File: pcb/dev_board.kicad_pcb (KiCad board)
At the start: 6 copper layers, 45.7 x 50 mm, 42 parts, among them J1 Conn_02x13_Odd_Even, J2 Conn_02x13_Odd_Even, J4 Conn_01x05, J5 Screw_Terminal_01x03, Q1 Si2356DS, Q2 Si2356DS, Q5 2N3906, Q6 MMBT3904, Q7 MMBT3906, SW1 SW_DIP_x04, U1 XS-LDT-01, U2 MAX5026, U3 KXTJ3-1057, U4 MCP1640BCH, U6 TLV74311

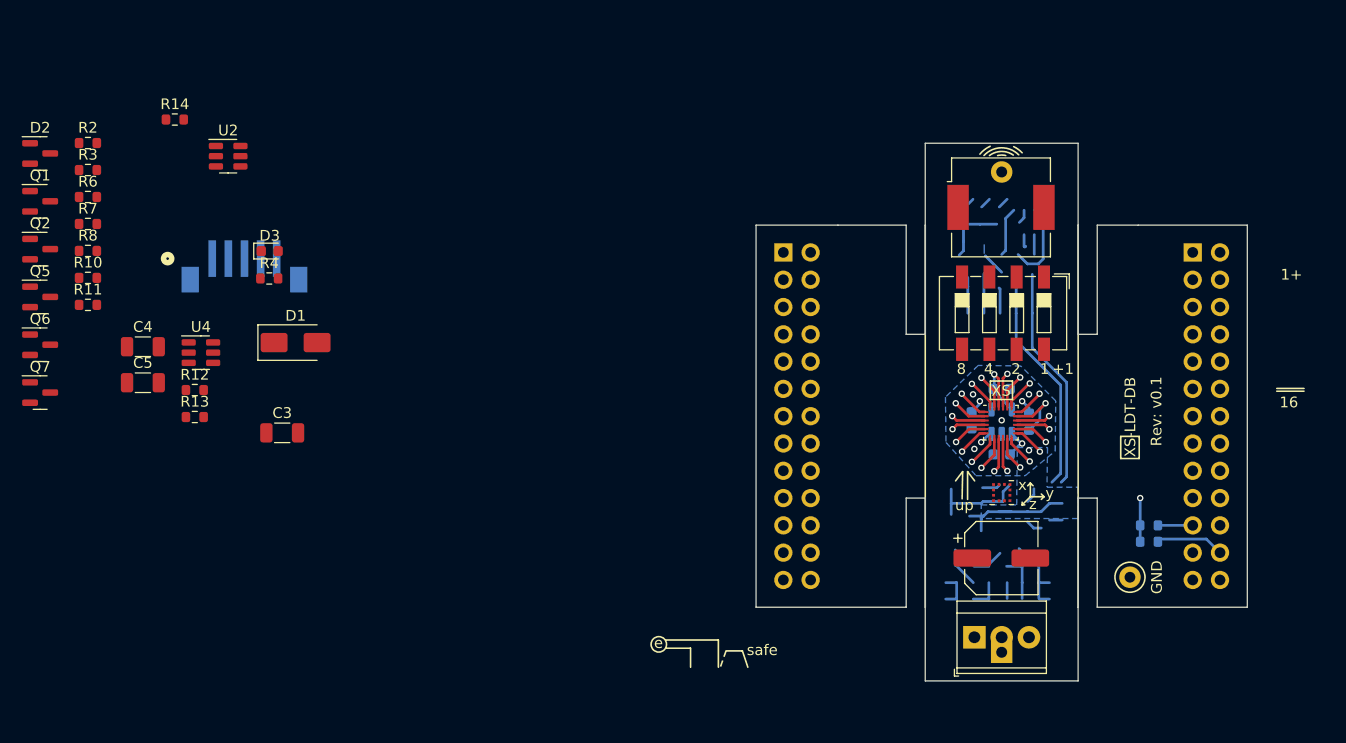
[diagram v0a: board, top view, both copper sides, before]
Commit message: V0.2 pcb placement, good enough to proceed/.
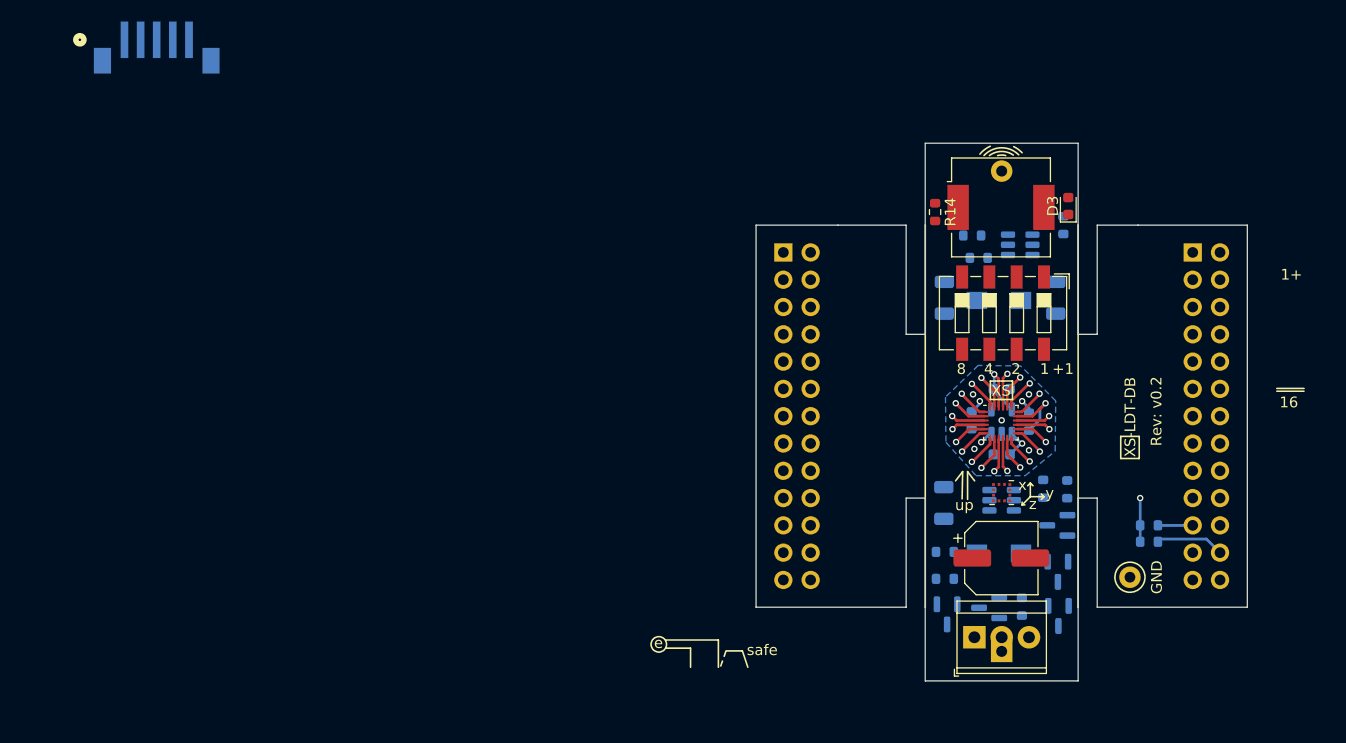
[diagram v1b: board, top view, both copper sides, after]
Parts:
- removed D1: ES1J, Diode_SMD:D_SMA
- removed Q5: 2N3906, Package_TO_SOT_SMD:SOT-23
- removed R2: 10K, Resistor_SMD:R_0603_1608Metric
- removed R6: 100K, Resistor_SMD:R_0603_1608Metric
- added L1: 47uH, Inductor_SMD:L_Wuerth_HCI-5040, B.Cu at (169.9, 116.9)
- added L2: 4.7uH, Inductor_SMD:L_Wuerth_HCI-5040, B.Cu at (169.9, 93.4)
- C3, C4, C5, D2, Q1, Q2, Q6, Q7, R10, R11, R12, R13, R3, R4, R7, R8, U2, U4: moved to B.Cu
- moved D2 100.8 mm to (175.4, 114.3), turned to 180 degrees
- moved Q2 100.7 mm to (175.5, 122.7), turned to -90 degrees
- moved Q7 96.2 mm to (175.4, 118.6), turned to -90 degrees
- moved R3 95.9 mm to (172.1, 121.9), turned to -90 degrees
- moved R10 93.2 mm to (176.3, 110.9), turned to -90 degrees
- moved Q1 92.7 mm to (165.1, 122.6), turned to -90 degrees
- moved Q6 91.6 mm to (169.0, 122.0), turned to 180 degrees
- moved R11 90.5 mm to (174.0, 110.9), turned to -90 degrees
- moved R7 85.4 mm to (164.9, 116.8), turned to 180 degrees
- moved R8 85.4 mm to (164.9, 119.3), turned to 180 degrees
- moved C5 85.3 mm to (175.2, 93.1), turned to -90 degrees
- moved U2 78.8 mm to (170.2, 112.0), turned to 180 degrees
- moved U4 76.9 mm to (171.9, 88.2), turned to 180 degrees
- moved C4 74.7 mm to (164.8, 93.1), turned to -90 degrees
- moved D3 74.4 mm to (176.4, 84.6), turned to 90 degrees
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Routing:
- net (no net): track 72.6 -> 16.4 mm
- net GND: track 31.9 -> 6.08 mm
- net unconnected-(J5-Pin_3-Pad3): track 18.5 -> 0.00 mm
- net unconnected-(J5-Pin_1-Pad1): track 15.3 -> 0.00 mm
- net +3.3V: track 21.0 -> 9.98 mm
- net /out: track 3.69 -> 0.00 mm
- net /pump: track 26.3 -> 23.3 mm
- net Net-(D3-K): track 1.02 -> 0.00 mm

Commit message: V0.3 schematic complete, footprints, 3d mods, prelim plancement. Ready for review then routing.
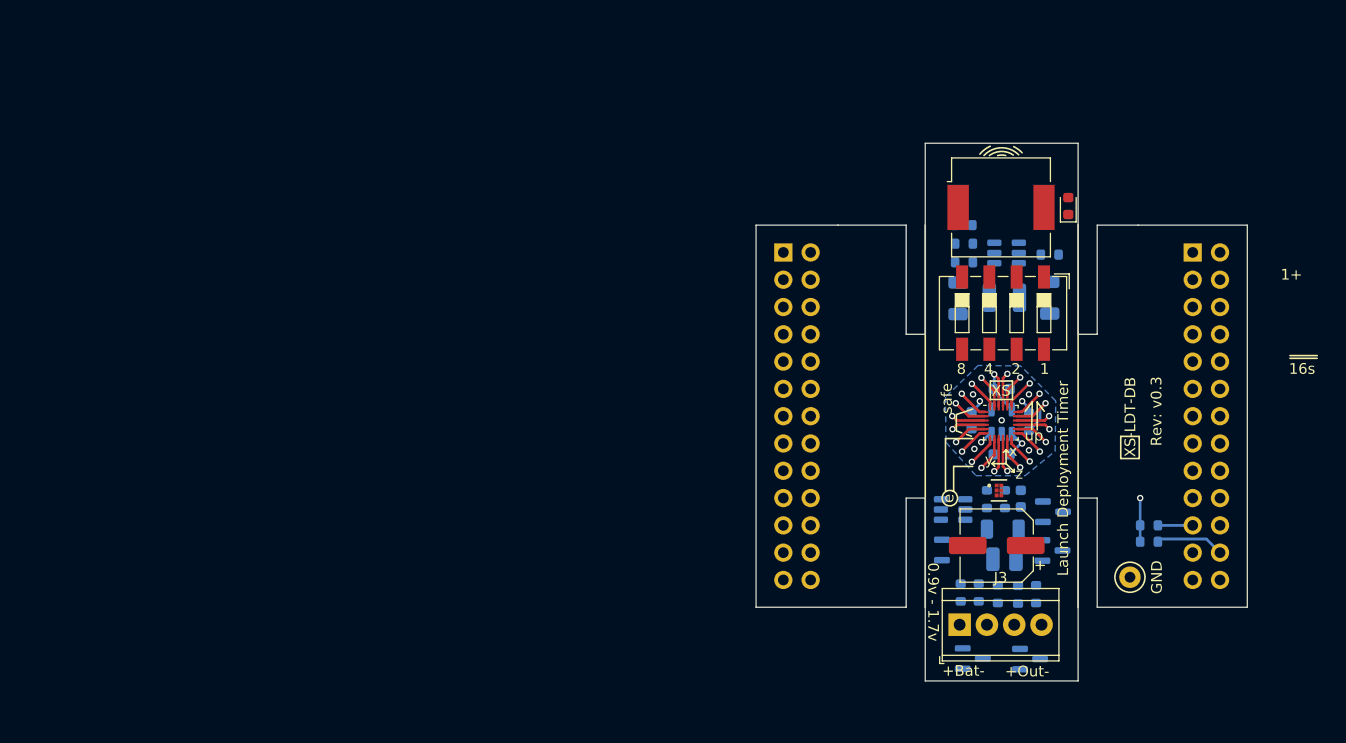
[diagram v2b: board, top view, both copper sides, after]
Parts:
- removed BT1: AAA Battery, Battery:BatteryHolder_Keystone_2466_1xAAA
- removed J4: Conn_01x05, Connector_JST:CONN_B5B-ZR-SM4-TF_JST
- removed J5: Screw_Terminal_01x03, TerminalBlock_TE-Connectivity:TerminalBlock_TE_282834-3_1x03_P2.54mm_Horizontal
- added C6: 1u, Capacitor_SMD:C_0603_1608Metric, B.Cu at (172.0, 111.8)
- added J3: Screw_Terminal_01x04, TerminalBlock_TE-Connectivity:TerminalBlock_TE_282834-4_1x04_P2.54mm_Horizontal, F.Cu at (166.3, 123.5)
- added R2: 3K3, Resistor_SMD:R_0603_1608Metric, B.Cu at (170.5, 111.9)
- added R6: 3K3, Resistor_SMD:R_0603_1608Metric, B.Cu at (168.8, 111.9)
- D2: value BAV99 -> CD0603-B0340R
- L1: footprint Inductor_SMD:L_Wuerth_HCI-5040 -> Inductor_SMD:L_1008_2520Metric
- L2: footprint Inductor_SMD:L_Wuerth_HCI-5040 -> Inductor_SMD:L_1210_3225Metric
- LS1: value Speaker -> Piezo
- R10: value 100K -> 147K
- R11: value 10K -> 6K34
- R12: value 100K -> 976K
- R13: value 10K -> 562K
- R14: moved to B.Cu
- U3: value KXTJ3-1057 -> MXC4005XC; footprint Package_LGA:Kionix_LGA-12_2x2mm_P0.5mm_LayoutBorder2x4y -> Sensor:MXC4005XC_MEM-M
- moved R11 12.3 mm to (166.4, 120.5), turned to 90 degrees
- moved R10 10.2 mm to (173.4, 120.7), turned to 90 degrees
- moved Q6 6.40 mm to (165.6, 116.6), turned to 0 degrees
- moved C3 6.00 mm to (170.3, 114.7), turned to 0 degrees
- moved R8 5.13 mm to (169.8, 120.7), turned to -90 degrees
- moved R7 4.92 mm to (168.0, 120.5), turned to -90 degrees
- moved Q2 4.80 mm to (172.8, 126.7), turned to 0 degrees
- moved Q1 4.76 mm to (167.5, 126.7), turned to 0 degrees
- moved U2 4.60 mm to (165.7, 112.8)
- moved R4 3.02 mm to (174.7, 89.1), turned to 0 degrees
- moved R14 2.91 mm to (166.6, 86.4), turned to 0 degrees
- moved Q7 2.05 mm to (174.9, 116.6), turned to 0 degrees
- moved U4 1.48 mm to (170.6, 89.0)
- moved R12 1.43 mm to (166.7, 89.8)
- moved D2 1.33 mm to (175.0, 113.0), turned to 0 degrees
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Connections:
- C1 pad 1: unconnected-(C1-Pad1) -> /cap_30v
- C1 pad 2: unconnected-(C1-Pad2) -> GND
- C3 pad 1: unconnected-(C3-Pad1) -> +3.3V
- C3 pad 2: unconnected-(C3-Pad2) -> GND
- C4 pad 1: unconnected-(C4-Pad1) -> +BATT
- C4 pad 2: unconnected-(C4-Pad2) -> GND
- C5 pad 1: unconnected-(C5-Pad1) -> +3.3V
- C5 pad 2: unconnected-(C5-Pad2) -> GND
- D2 pad 1: unconnected-(D2-K-Pad1) -> /cap_30v
- D2 pad 2: unconnected-(D2-A-Pad2) -> Net-(D2-A)
- D2 pad 3: unconnected-(D2-K-Pad3) -> (no net)
- D3 pad 2: /run_led -> /status_led
- J1 pad 18: Net-(J1-Pin_18) -> /sw2
- J1 pad 20: /start -> /sw3
- J1 pad 6: /setup -> /sw4
- J2 pad 11: /run_led -> /scl
- J2 pad 13: /fault_led -> /sda
- J2 pad 15: /time_led -> /cont_en
- J2 pad 17: Net-(J2-Pin_17) -> /cont_sns
- J2 pad 19: /adc_clk -> /deploy
- J2 pad 21: /adc_miso -> /dump
- J2 pad 23: /adc_mosi -> /charge
- J2 pad 25: /adc_ncs -> /sw1
- J2 pad 5: /period -> /speaker+
- J2 pad 7: /pump -> /speaker-
- J2 pad 9: /timeout -> /status_led
- L1 pad 1: unconnected-(L1-Pad1) -> +3.3V
- L1 pad 2: unconnected-(L1-Pad2) -> Net-(D2-A)
- L2 pad 1: unconnected-(L2-Pad1) -> +BATT
- L2 pad 2: unconnected-(L2-Pad2) -> Net-(U4-SW)
- LS1 pad 1: unconnected-(LS1-Pad1) -> /speaker+
- LS1 pad 2: unconnected-(LS1-Pad2) -> /speaker-
- Q1 pad 1: unconnected-(Q1-G-Pad1) -> /dump
- Q1 pad 2: unconnected-(Q1-S-Pad2) -> GND
- Q1 pad 3: unconnected-(Q1-D-Pad3) -> /cap_30v
- Q2 pad 1: unconnected-(Q2-G-Pad1) -> /deploy
- Q2 pad 2: unconnected-(Q2-S-Pad2) -> GND
- Q2 pad 3: unconnected-(Q2-D-Pad3) -> Net-(J3-Pin_4)
- Q6 pad 1: unconnected-(Q6-B-Pad1) -> Net-(Q6-B)
- Q6 pad 2: unconnected-(Q6-E-Pad2) -> GND
- Q6 pad 3: unconnected-(Q6-C-Pad3) -> /cont_sns
- Q7 pad 1: unconnected-(Q7-B-Pad1) -> Net-(Q7-B)
- Q7 pad 2: unconnected-(Q7-E-Pad2) -> +3.3V
- Q7 pad 3: unconnected-(Q7-C-Pad3) -> Net-(Q7-C)
- R10 pad 1: unconnected-(R10-Pad1) -> Net-(U2-FB)
- R10 pad 2: unconnected-(R10-Pad2) -> /cap_30v
- R11 pad 1: unconnected-(R11-Pad1) -> GND
- R11 pad 2: unconnected-(R11-Pad2) -> Net-(U2-FB)
- R12 pad 1: unconnected-(R12-Pad1) -> Net-(U4-VFB)
- R12 pad 2: unconnected-(R12-Pad2) -> +3.3V
- R13 pad 1: unconnected-(R13-Pad1) -> GND
- R13 pad 2: unconnected-(R13-Pad2) -> Net-(U4-VFB)
- R14 pad 1: unconnected-(R14-Pad1) -> Net-(Q7-B)
- R14 pad 2: unconnected-(R14-Pad2) -> /cont_en
- R3 pad 1: unconnected-(R3-Pad1) -> Net-(J3-Pin_4)
- R3 pad 2: unconnected-(R3-Pad2) -> Net-(Q7-C)
- R7 pad 1: unconnected-(R7-Pad1) -> Net-(Q6-B)
- R7 pad 2: unconnected-(R7-Pad2) -> Net-(J3-Pin_4)
- R8 pad 1: unconnected-(R8-Pad1) -> /cont_sns
- R8 pad 2: unconnected-(R8-Pad2) -> +3.3V
- U1 pad 1: /timeout -> /status_led
- U1 pad 13: /start -> /sw3
- U1 pad 14: Net-(J1-Pin_18) -> /sw2
- U1 pad 2: /run_led -> /scl
- U1 pad 20: /setup -> /sw4
- U1 pad 23: /period -> /speaker+
- U1 pad 24: /pump -> /speaker-
- U1 pad 3: /fault_led -> /sda
- U1 pad 4: /time_led -> /cont_en
- U1 pad 5: Net-(J2-Pin_17) -> /cont_sns
- U1 pad 6: /adc_clk -> /deploy
- U1 pad 7: /adc_miso -> /dump
- U1 pad 8: /adc_mosi -> /charge
- U1 pad 9: /adc_ncs -> /sw1
- U2 pad 1: unconnected-(U2-SW-Pad1) -> GND
- U2 pad 2: unconnected-(U2-GND-Pad2) -> GND
- U2 pad 3: unconnected-(U2-FB-Pad3) -> Net-(U2-FB)
- U2 pad 4: unconnected-(U2-EN-Pad4) -> /charge
- U2 pad 5: unconnected-(U2-IN-Pad5) -> +3.3V
- U2 pad 6: unconnected-(U2-NC-Pad6) -> Net-(D2-A)
- U3 pad 1: unconnected-(U3-ADDR-Pad1) -> /scl
- U3 pad 3: Net-(U3-IO_VDD-Pad11) -> GND
- U3 pad 5: unconnected-(U3-INT-Pad5) -> /sda
- U3 pad 6: Net-(U3-GND-Pad6) -> +3.3V
- U4 pad 1: unconnected-(U4-SW-Pad1) -> Net-(U4-SW)
- U4 pad 2: unconnected-(U4-GND-Pad2) -> GND
- U4 pad 3: unconnected-(U4-EN-Pad3) -> +BATT
- U4 pad 4: unconnected-(U4-VFB-Pad4) -> Net-(U4-VFB)
- U4 pad 5: unconnected-(U4-VOUT-Pad5) -> +3.3V
- U4 pad 6: unconnected-(U4-VIN-Pad6) -> +BATT
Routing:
- net /adc_ncs: track 27.0 -> 0.00 mm, vias 1 -> 0
- net /sw1: track 0.00 -> 27.0 mm, vias 0 -> 1
- net /sw4: track 0.00 -> 25.5 mm, vias 0 -> 1
- net /setup: track 25.5 -> 0.00 mm, vias 1 -> 0
- net /speaker+: track 0.00 -> 25.3 mm, vias 0 -> 1
- net /period: track 25.3 -> 0.00 mm, vias 1 -> 0
- net /charge: track 0.00 -> 24.9 mm, vias 0 -> 1
- net /adc_mosi: track 24.9 -> 0.00 mm, vias 1 -> 0
- net /speaker-: track 0.00 -> 23.3 mm, vias 0 -> 1
- net /pump: track 23.3 -> 0.00 mm, vias 1 -> 0
- net /dump: track 0.00 -> 22.9 mm, vias 0 -> 1
- net /adc_miso: track 22.9 -> 0.00 mm, vias 1 -> 0
- net /timeout: track 21.7 -> 0.00 mm, vias 1 -> 0
- net /status_led: track 0.00 -> 21.7 mm, vias 0 -> 1
- net /sw3: track 0.00 -> 21.4 mm, vias 0 -> 1
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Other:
- board text added: "+Bat-"
- board text added: "+Out-"
- board text added: "0.9v - 1.7v"
- board text added: "16s"
- board text added: "Launch Deployment Timer"
- board text removed: "+1"
- board text removed: "16"

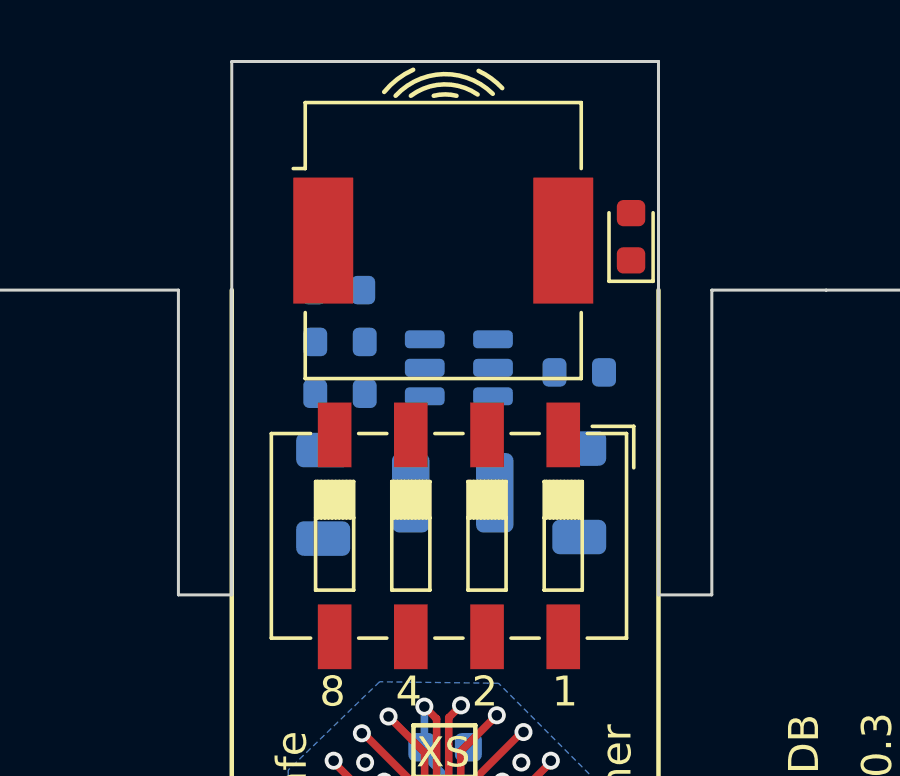
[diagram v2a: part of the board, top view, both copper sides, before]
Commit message: Added Fram in soic-8 as flight recorder for validation flights
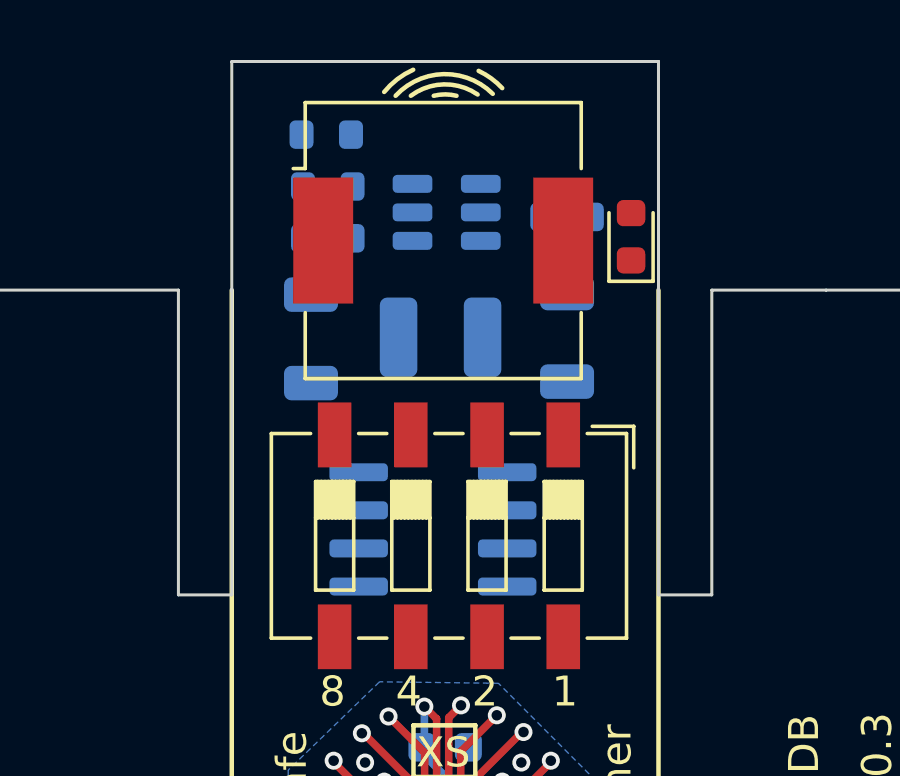
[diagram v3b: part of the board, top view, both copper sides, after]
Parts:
- added U7: FM24W256, Package_SO:SOIC-8_3.9x4.9mm_P1.27mm, B.Cu at (169.8, 94.3)
- R9: value 3k3 -> 3K3
- moved U4 5.20 mm to (170.2, 83.8)
- moved C5 5.20 mm to (174.2, 87.9)
- moved L2 5.20 mm to (170.0, 87.9)
- moved R12 5.20 mm to (166.3, 84.6)
- moved R14 5.20 mm to (166.2, 81.2)
- moved R4 5.20 mm to (174.2, 83.9)
- moved C4 5.20 mm to (165.7, 88.0)
- moved R13 5.20 mm to (166.3, 82.9)

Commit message: pcb v0.5 added fram, and isp hdr, first place and route, assigned chip i/o to match routing.
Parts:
- added C7: 0.1u, Capacitor_SMD:C_0603_1608Metric, B.Cu at (165.6, 96.1)
- added J4: Conn_01x05, Connector_JST:CONN_B5B-ZR-SM4-TF_JST, B.Cu at (170.1, 82.3)
- added R15: 3K3, Resistor_SMD:R_0603_1608Metric, B.Cu at (164.2, 88.4)
- D2: footprint Package_TO_SOT_SMD:SOT-23 -> Diode_SMD:D_0603_1608Metric
- moved R14 44.7 mm to (168.7, 125.9), turned to 180 degrees
- moved R6 17.9 mm to (174.8, 95.0)
- moved R2 14.4 mm to (174.8, 98.1)
- moved R13 11.7 mm to (173.4, 92.3)
- moved R7 8.75 mm to (175.0, 125.9), turned to 180 degrees
- moved R12 8.33 mm to (171.0, 91.5), turned to 90 degrees
- moved Q1 7.97 mm to (171.8, 120.0), turned to 90 degrees
- moved Q7 7.33 mm to (168.4, 120.0), turned to 90 degrees
- moved Q2 7.16 mm to (175.3, 120.0), turned to 90 degrees
- moved R11 7.12 mm to (172.6, 117.1), turned to 180 degrees
- moved R8 6.74 mm to (165.5, 125.9), turned to 180 degrees
- moved R10 5.89 mm to (173.4, 114.8)
- moved L1 5.61 mm to (169.7, 111.9), turned to 0 degrees
- moved R3 5.11 mm to (171.8, 125.9), turned to 180 degrees
- moved R4 4.98 mm to (176.1, 88.5), turned to -90 degrees
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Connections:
- J1 pad 18: /sw2 -> /deploy
- J1 pad 20: /sw3 -> /dump
- J1 pad 6: /sw4 -> /sw1
- J2 pad 11: /scl -> /speaker-
- J2 pad 13: /sda -> /speaker+
- J2 pad 15: /cont_en -> /sw4
- J2 pad 17: /cont_sns -> /cont_en
- J2 pad 19: /deploy -> /cont_sns
- J2 pad 21: /dump -> /charge
- J2 pad 23: /charge -> /scl
- J2 pad 25: /sw1 -> /sda
- J2 pad 5: /speaker+ -> /sw2
- J2 pad 7: /speaker- -> /sw3
- U1 pad 13: /sw3 -> /dump
- U1 pad 14: /sw2 -> /deploy
- U1 pad 2: /scl -> /speaker-
- U1 pad 20: /sw4 -> /sw1
- U1 pad 23: /speaker+ -> /sw2
- U1 pad 24: /speaker- -> /sw3
- U1 pad 3: /sda -> /speaker+
- U1 pad 4: /cont_en -> /sw4
- U1 pad 5: /cont_sns -> /cont_en
- U1 pad 6: /deploy -> /cont_sns
- U1 pad 7: /dump -> /charge
- U1 pad 8: /charge -> /scl
- U1 pad 9: /sw1 -> /sda
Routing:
- net /sda: track 19.9 -> 66.0 mm, vias 1 -> 3
- net +BATT: track 0.00 -> 45.0 mm, vias 0 -> 1
- net GND: track 6.08 -> 48.7 mm, vias 6 -> 24
- net /scl: track 20.8 -> 61.1 mm, vias 1 -> 3
- net /reset_n: track 19.9 -> 58.4 mm, vias 2 -> 3
- net /cont_en: track 19.5 -> 46.8 mm
- net +3.3V: track 9.98 -> 35.9 mm, vias 5 -> 16
- net /status_led: track 21.7 -> 46.4 mm
- net /cont_sns: track 20.4 -> 41.9 mm
- net /cap_30v: track 0.00 -> 20.9 mm
- net /speaker-: track 23.3 -> 42.5 mm
- net Net-(Q6-B): track 0.00 -> 16.7 mm
- net /speaker+: track 25.3 -> 41.9 mm
- net /deploy: track 21.3 -> 35.7 mm
- net /dump: track 22.9 -> 37.1 mm
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- removed copper zone on In4.Cu, net (none)

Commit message: PCB v0.7 schem, pdf, pcb, gerbs
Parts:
- added C8: 0.1u, Capacitor_SMD:C_0603_1608Metric, B.Cu at (182.3, 110.1)
- added R16: dni, Resistor_SMD:R_0603_1608Metric, B.Cu at (180.3, 99.5)
- added TP2: GND, TestPoint:TestPoint_Keystone_5000-5004_Miniature, F.Cu at (158.3, 89.3)
- added X1: ASE-48MHz, Oscillator:Oscillator_SMD_Abracon_ASV-4Pin_7.0x5.1mm_HandSoldering, B.Cu at (182.1, 104.7)
- moved R13 3.97 mm to (174.7, 88.5), turned to 90 degrees
- moved C5 3.87 mm to (172.5, 91.8), turned to 0 degrees
- moved R12 3.65 mm to (173.1, 88.5), turned to -90 degrees
- moved C6 2.36 mm to (170.3, 111.1)
- moved L1 2.33 mm to (167.4, 111.5)
- moved C3 0.27 mm to (166.3, 115.4)
- turned C4 to 0 degrees
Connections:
- U3 pad 2: unconnected-(U3-nc-Pad2) -> /nc_nc
- U3 pad 4: unconnected-(U3-INT-Pad4) -> /nc_int
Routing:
- net +3.3V: track 35.9 -> 50.8 mm, vias 16 -> 19
- net +BATT: track 45.0 -> 58.8 mm, vias 1 -> 2
- net GND: track 48.7 -> 58.7 mm, vias 24 -> 28
- net /osc: track 19.6 -> 25.5 mm, vias 1 -> 2
- net Net-(X1-OUT): track 0.00 -> 2.59 mm
- net Net-(U4-VFB): track 5.32 -> 3.68 mm
- net /sda: track 66.0 -> 67.2 mm, vias 3 -> 4
- net Net-(D2-A): track 3.93 -> 4.93 mm
- net /charge: track 33.8 -> 34.8 mm
- net /speaker-: track 42.5 -> 43.3 mm
- net /sw2: track 29.7 -> 30.5 mm
- net /cont_en: track 46.8 -> 46.2 mm
- net /sw1: track 29.1 -> 29.6 mm
- added copper zone on F.Cu, net +3.3V
- added copper zone on F.Cu, net /nc_int
- added copper zone on F.Cu, net /nc_nc
- added copper zone on F.Cu, net /scl
- added copper zone on F.Cu, net /sda
- added copper zone on F.Cu, net GND
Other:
- board text added: "c Eric Pearson 2026"
- board text removed: "(c) Eric Pearson 2026"
- board text removed: "1+"
- board text removed: "16s"

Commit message: Update to v0.8 pcb, sch, bom, gerbs, pdf. Tapeout candidate?
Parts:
- added R23: dni, Resistor_SMD:R_0603_1608Metric, B.Cu at (183.9, 112.8)
- added U5: AT25xxx, Package_SO:SOIC-8_3.9x4.9mm_P1.27mm, B.Cu at (182.6, 92.7)
- added U8: LM809, Package_TO_SOT_SMD:SOT-23, B.Cu at (183.9, 118.8)
- moved TP1 1.48 mm to (181.2, 118.0)
- moved TP2 0.99 mm to (158.9, 90.1)
- moved X1 0.26 mm to (182.1, 105.0)
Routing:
- net /spi_ss: track 24.3 -> 37.0 mm, vias 1 -> 2
- net /spi_ck: track 20.1 -> 28.2 mm, vias 1 -> 2
- net /spi_so: track 23.5 -> 30.7 mm, vias 1 -> 2
- net Net-(U8-~{RESET}): track 0.00 -> 6.49 mm
- net GND: track 58.7 -> 62.1 mm, vias 28 -> 29
- net /spi_si: track 21.9 -> 24.8 mm, vias 1 -> 2
- net +3.3V: track 50.8 -> 53.7 mm, vias 19 -> 21
